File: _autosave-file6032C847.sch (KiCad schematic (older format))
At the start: 7 parts

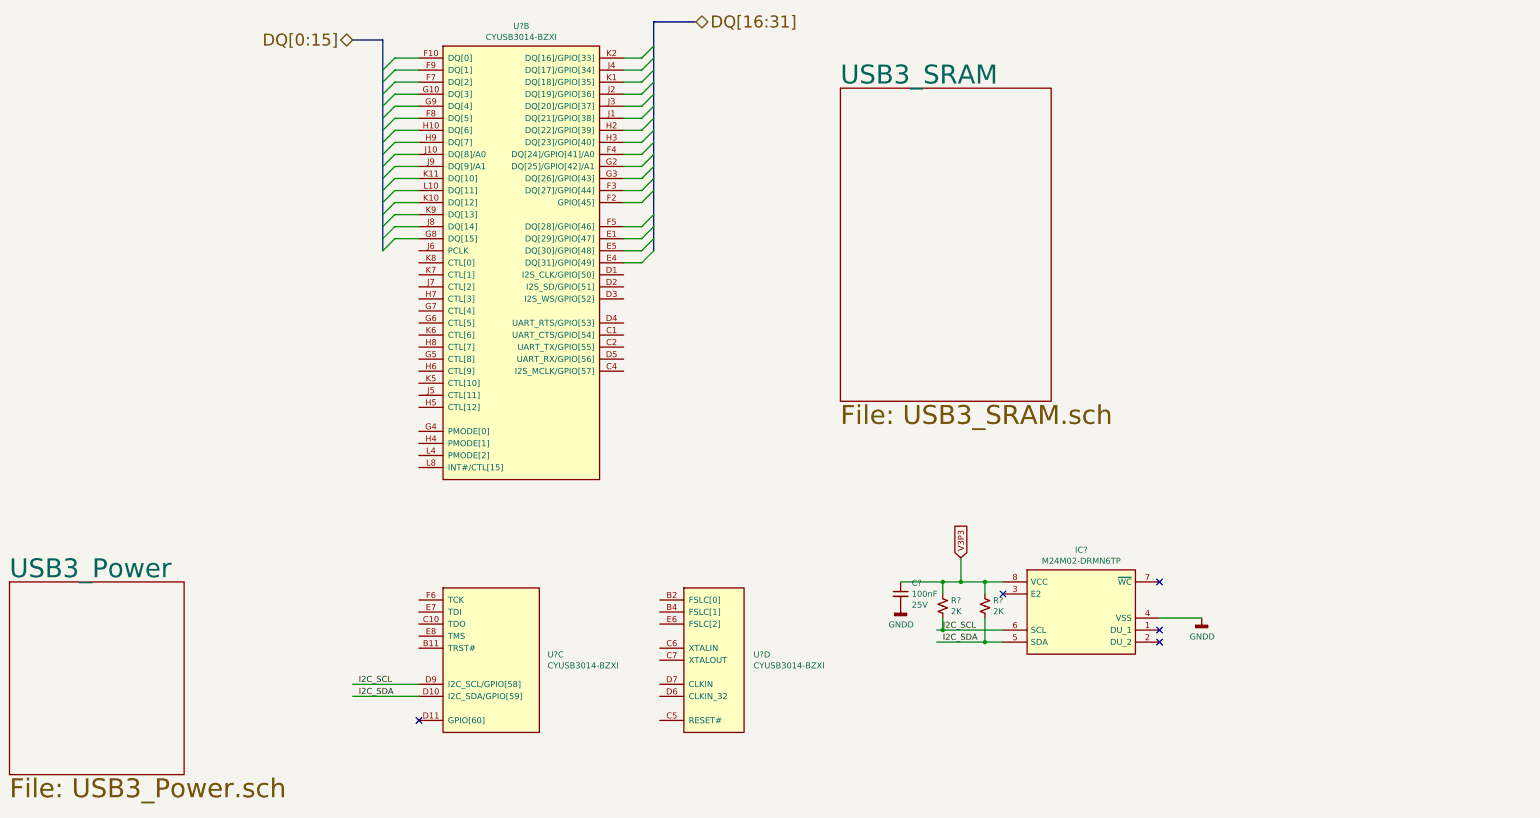
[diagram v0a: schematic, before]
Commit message: Added USB3 SRAM Added 5V regulator
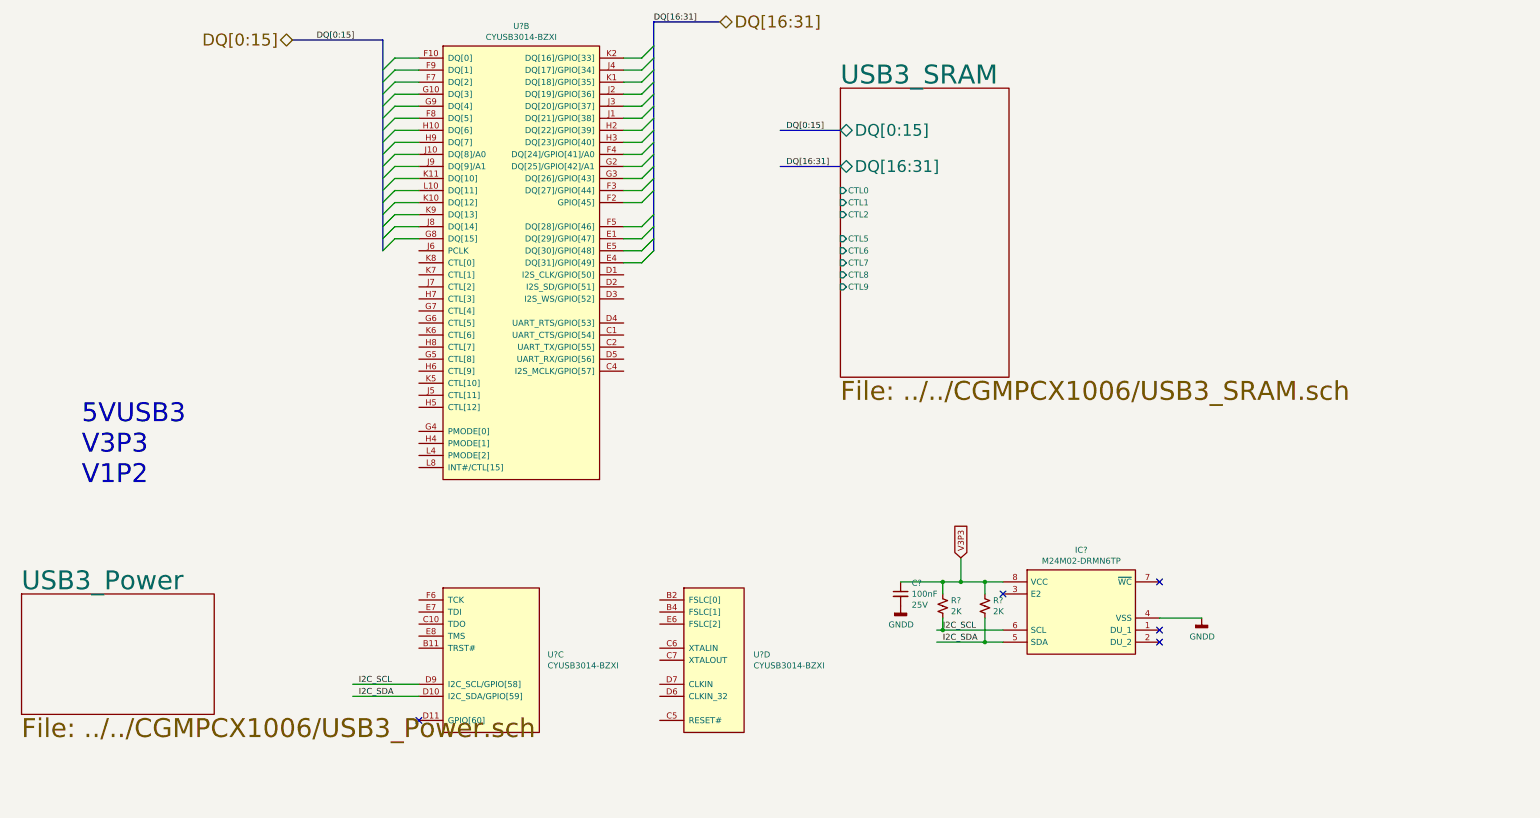
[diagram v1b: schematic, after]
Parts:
- removed R?: 2K, Resistor_SMD:R_0603_1608Metric_Pad0.98x0.95mm_HandSolder, symbol Device:R_Small_US
- added R?: 2K, Resistor_SMD:R_0603_1608Metric_Pad0.98x0.95mm_HandSolder, symbol Device:R_Small_US
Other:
- note added: "5VUSB3\nV3P3\nV1P2"
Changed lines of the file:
@@
 EELAYER 30 0
 EELAYER END
-$Descr A4 11693 8268
+$Descr A3 16535 11693
 encoding utf-8
-Sheet 7 19
-Title "CGMPCX1006"
-Date "2021-02-03"
-Rev "V1"
-Comp "Glowmagik Innovations"
+Sheet 19 21
+Title ""
+Date ""
+Rev ""
+Comp ""
 Comment1 ""
 Comment2 ""
@@
 $EndDescr
 $Sheet
-S 750  5700 1450 1600
+S 850  5800 1600 1000
 U 60277424
 F0 "USB3_Power" 157
-F1 "USB3_Power.sch" 157
-$EndSheet
-$Sheet
-S 7650 1600 1750 2600
-U 603A73D8
-F0 "USB3_SRAM" 157
-F1 "USB3_SRAM.sch" 157
+F1 "../../CGMPCX1006/USB3_Power.sch" 157
 $EndSheet
 $Comp
@@
 	5850 2950 6000 2950
 Wire Bus Line
-	3850 1200 3600 1200
-Wire Bus Line
-	6100 1050 6450 1050
-Text HLabel 3600 1200 0    100  BiDi ~ 0
+	3850 1200 3100 1200
+Wire Bus Line
+	6100 1050 6650 1050
+Text HLabel 3100 1200 0    100  BiDi ~ 0
 DQ[0:15]
-Text HLabel 6450 1050 2    100  BiDi ~ 0
+Text HLabel 6650 1050 2    100  BiDi ~ 0
 DQ[16:31]
 $Comp
@@
 $Comp
 L Device:R_Small_US R?
-U 1 1 603FAEC1
+U 1 1 603E3C81
 P 8850 5900
 F 0 "R?" H 8918 5946 50  0000 L CNN
@@
 	8850 5700 8650 5700
 NoConn ~ 4150 6850
+Text Label 6100 1050 0    50   ~ 0
+DQ[16:31]
+Text Label 3300 1200 0    50   ~ 0
+DQ[0:15]
+Wire Bus Line
+	7650 2250 7150 2250
+Wire Bus Line
+	7650 1950 7150 1950
+Text Label 7200 1950 0    50   ~ 0
+DQ[0:15]
+Text Label 7200 2250 0    50   ~ 0
+DQ[16:31]
+Text Notes 1350 4900 0    157  ~ 0
+5VUSB3\nV3P3\nV1P2
+$Sheet
+S 7650 1600 1400 2400
+U 603E3C7E
+F0 "USB3_SRAM" 157
+F1 "../../CGMPCX1006/USB3_SRAM.sch" 157
+F2 "DQ[0:15]" B L 7650 1950 98
+F3 "DQ[16:31]" B L 7650 2250 98
+F4 "CTL0" I L 7650 2450 50
+F5 "CTL1" I L 7650 2550 50
+F6 "CTL2" I L 7650 2650 50
+F7 "CTL5" I L 7650 2850 50
+F8 "CTL6" I L 7650 2950 50
+F9 "CTL7" I L 7650 3050 50
+F10 "CTL8" I L 7650 3150 50
+F11 "CTL9" I L 7650 3250 50
+$EndSheet
+Wire Bus Line
+	6100 1050 6100 2950
 Wire Bus Line
 	3850 1200 3850 2950
-Wire Bus Line
-	6100 1050 6100 2950
 $EndSCHEMATC
